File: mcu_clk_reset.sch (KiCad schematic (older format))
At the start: 52 parts, among them J4 20021121-00010C4LF, J5 M20-8762042, Q3 BSS214NW, Q4 BSS214NW, Q5 BSS214NW, Q6 BSS214NW, U4 IS25WP032D, U5 FE310-G002, X1 KX2132709Z, Y1 TSX-3225 16.0000MF18X-AC0

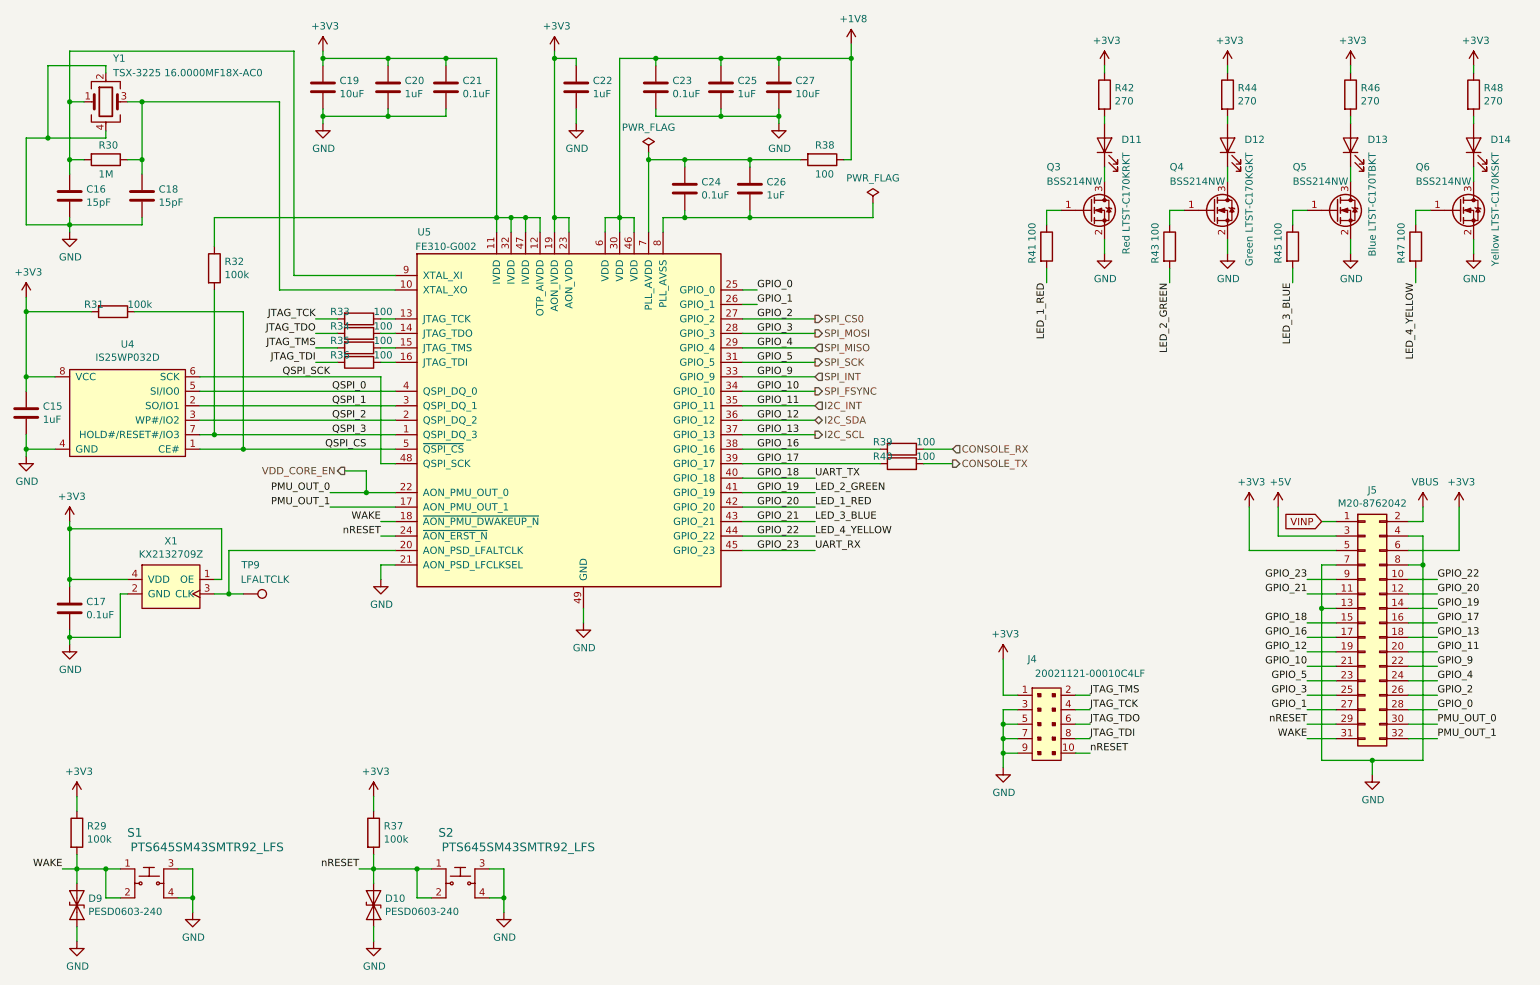
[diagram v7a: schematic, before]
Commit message: Placed MCU decoupling capacitors
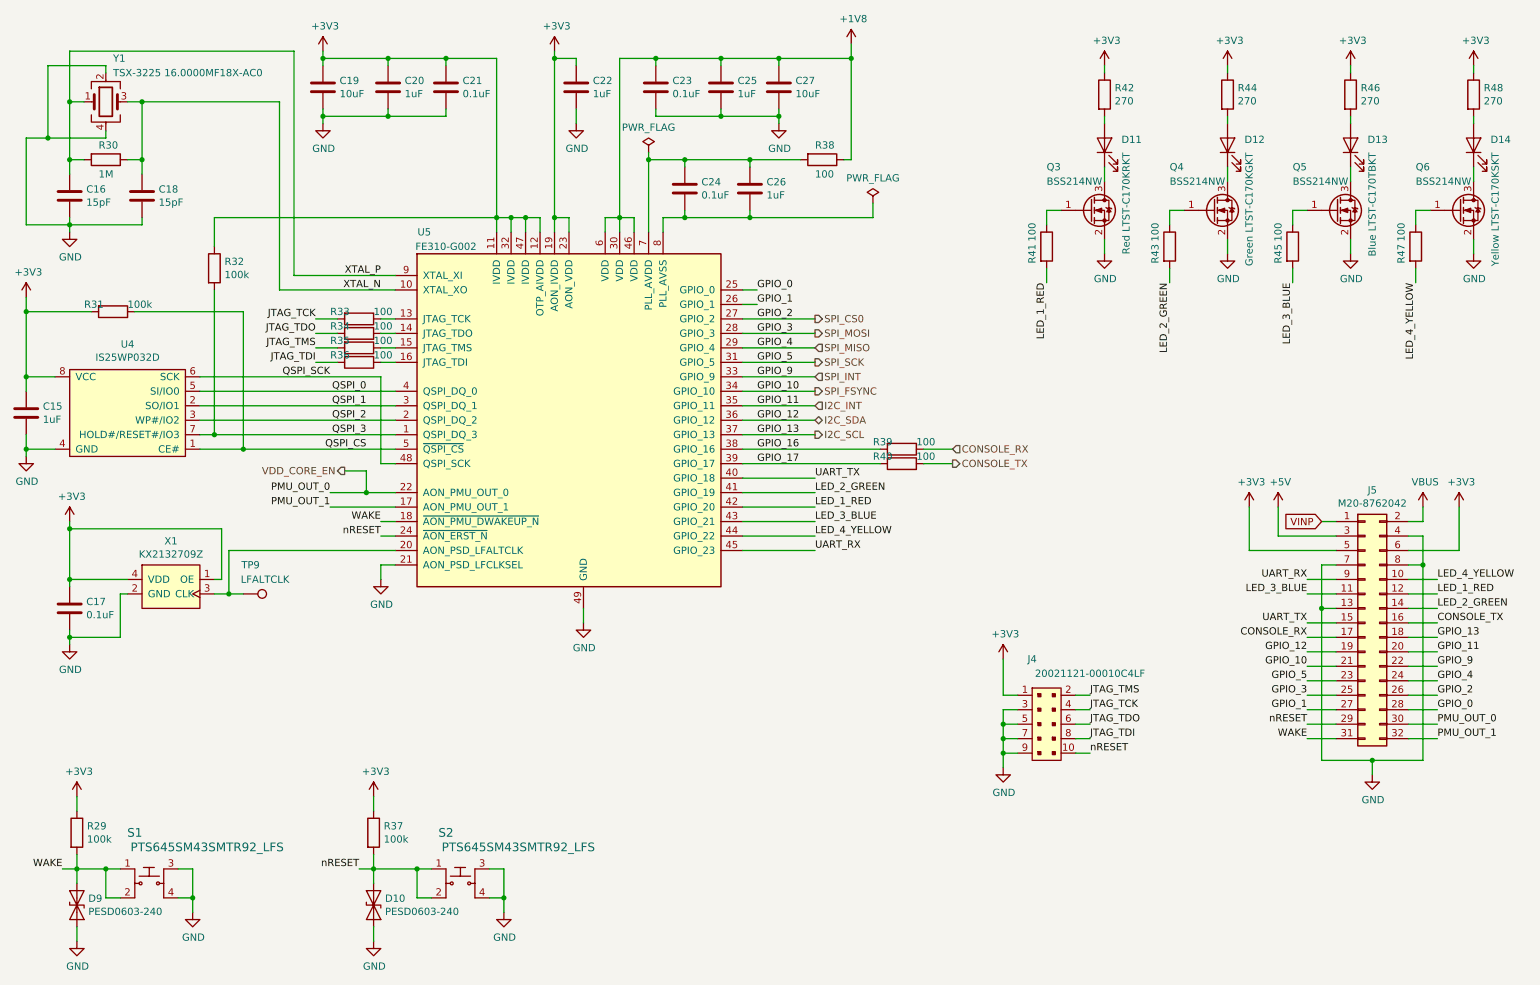
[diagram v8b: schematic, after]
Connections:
- net CONSOLE_RX: now also J5.17 (Pin_17)
- net CONSOLE_TX: now also J5.16 (Pin_16)
- net GPIO_16: no longer J5.17 (Pin_17)
- net GPIO_17: no longer J5.16 (Pin_16)
- net XTAL_N: now reaches C18.1, R30.1, U5.10 (XTAL_XO), Y1.3
- net XTAL_P: now reaches C16.1, R30.2, U5.9 (XTAL_XI), Y1.1
- net GPIO_18 renamed UART_TX
- net GPIO_19 renamed LED_2_GREEN
- net GPIO_20 renamed LED_1_RED
- net GPIO_21 renamed LED_3_BLUE
- net GPIO_22 renamed LED_4_YELLOW
- net GPIO_23 renamed UART_RX
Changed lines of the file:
@@
 GPIO_17
 Text Label 10400 4800 0    50   ~ 0
-GPIO_17
+CONSOLE_TX
 Text Label 9500 4900 2    50   ~ 0
-GPIO_16
+CONSOLE_RX
 Text Label 10400 4900 0    50   ~ 0
 GPIO_13
@@
 Wire Wire Line
 	5600 4300 6100 4300
-Text Label 5700 3800 0    50   ~ 0
-GPIO_18
-Text Label 5700 3900 0    50   ~ 0
-GPIO_19
-Text Label 5700 4000 0    50   ~ 0
-GPIO_20
-Text Label 5700 4100 0    50   ~ 0
-GPIO_21
-Text Label 5700 4200 0    50   ~ 0
-GPIO_22
-Text Label 5700 4300 0    50   ~ 0
-GPIO_23
-Text Label 9500 4800 2    50   ~ 0
-GPIO_18
-Text Label 10400 4700 0    50   ~ 0
-GPIO_19
-Text Label 10400 4600 0    50   ~ 0
-GPIO_20
-Text Label 9500 4600 2    50   ~ 0
-GPIO_21
-Text Label 10400 4500 0    50   ~ 0
-GPIO_22
-Text Label 9500 4500 2    50   ~ 0
-GPIO_23
 Wire Wire Line
 	8950 950  8950 1000
@@
 Text Label 2750 3100 2    50   ~ 0
 QSPI_SCK
+Text Label 9500 4800 2    50   ~ 0
+UART_TX
+Text Label 10400 4700 0    50   ~ 0
+LED_2_GREEN
+Text Label 10400 4600 0    50   ~ 0
+LED_1_RED
+Text Label 9500 4600 2    50   ~ 0
+LED_3_BLUE
+Text Label 10400 4500 0    50   ~ 0
+LED_4_YELLOW
+Text Label 9500 4500 2    50   ~ 0
+UART_RX
+Text Label 3100 2400 2    50   ~ 0
+XTAL_P
+Text Label 3100 2500 2    50   ~ 0
+XTAL_N
 $EndSCHEMATC
